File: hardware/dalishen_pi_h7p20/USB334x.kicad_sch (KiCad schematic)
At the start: 20 parts, among them J2 USB_C_Receptacle_USB2.0_16P, J3 USB_A, SW6 SW_DPDT_x2, U20 USB3343, Y1 26M

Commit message: [dalishen_pi_h7p20] Backup
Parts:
- added F4: SMD0805B100TFT, Fuse:Fuse_0805_2012Metric, symbol Device:Polyfuse
- SW6: footprint (none) -> Button_Switch_SMD:SW_DIP_SPSTx03_Slide_KingTek_DSHP03TJ_W5.25mm_P1.27mm_JPin
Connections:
- net T_VBUS: now also F4.1; no longer J2.A4 (VBUS), J2.A9 (VBUS), J2.B4 (VBUS), J2.B9 (VBUS), J3.1 (VBUS)
- new net: F4.2, J2.A4 (VBUS), J2.A9 (VBUS), J2.B4 (VBUS), J2.B9 (VBUS), J3.1 (VBUS)
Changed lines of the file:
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@@
 	(wire
 		(pts
-			(xy 146.05 53.34) (xy 120.65 53.34)
+			(xy 146.05 53.34) (xy 137.16 53.34)
 		)
 		(stroke
@@
 	(wire
 		(pts
+			(xy 129.54 53.34) (xy 120.65 53.34)
+		)
+		(stroke
+			(width 0)
+			(type default)
+		)
+	)
+	(wire
+		(pts
 			(xy 154.94 93.98) (xy 154.94 95.25)
 		)
@@
 	)
 	(label "T_VBUS"
-		(at 109.22 107.95 0)
+		(at 137.16 53.34 0)
 		(effects
 			(font
@@
 	)
 	(symbol
+		(lib_id "Device:Polyfuse")
+		(at 133.35 53.34 270)
+		(unit 1)
+		(exclude_from_sim no)
+		(in_bom yes)
+		(on_board yes)
+		(dnp no)
+		(property "Reference" "F4"
+			(at 133.35 47.625 90)
+			(effects
+				(font
+					(size 1.27 1.27)
+				)
+			)
+		)
+		(property "Value" "SMD0805B100TFT"
+			(at 133.35 49.9364 90)
+			(effects
+				(font
+					(size 1.27 1.27)
+				)
+			)
+		)
+		(property "Footprint" "Fuse:Fuse_0805_2012Metric"
+			(at 128.27 54.61 0)
+			(effects
+				(font
+					(size 1.27 1.27)
+				)
+				(justify left)
+				(hide yes)
+			)
+		)
+		(property "Datasheet" "~"
+			(at 133.35 53.34 0)
+			(effects
+				(font
+					(size 1.27 1.27)
+				)
+				(hide yes)
+			)
+		)
+		(property "Description" ""
+			(at 133.35 53.34 0)
+			(effects
+				(font
+					(size 1.27 1.27)
+				)
+			)
+		)
+		(pin "1"
+		)
+		(pin "2"
+		)
+		(instances
+			(project "dalishen_pi_h7p20"
+				(path "/221176f3-b6da-4f04-afa6-f8c6dd49907a/c2e39904-e110-4fb2-9a78-c219110dbd62"
+					(reference "F4")
+					(unit 1)
+				)
+			)
+		)
+	)
+	(symbol
 		(lib_id "Device:R")
 		(at 48.26 62.23 270)
@@
 			)
 		)
-		(property "Footprint" ""
+		(property "Footprint" "Button_Switch_SMD:SW_DIP_SPSTx03_Slide_KingTek_DSHP03TJ_W5.25mm_P1.27mm_JPin"
 			(at 38.1 59.69 0)
 			(effects
@@
 			)
 		)
-		(property "Footprint" ""
+		(property "Footprint" "Button_Switch_SMD:SW_DIP_SPSTx03_Slide_KingTek_DSHP03TJ_W5.25mm_P1.27mm_JPin"
 			(at 38.1 46.99 0)
 			(effects

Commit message: [dalishen_pi_h7p20] 待review
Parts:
- SW6: footprint Button_Switch_SMD:SW_DIP_SPSTx03_Slide_KingTek_DSHP03TJ_W5.25mm_P1.27mm_JPin -> vllogic:SW_PUSH_5.8mm_LOCK_SMT
- U20: footprint Package_DFN_QFN:QFN-24-1EP_4x4mm_P0.5mm_EP2.6x2.6mm -> vllogic:QFN-24-1EP_4x4mm_P0.5mm_EP2.6x2.6mm
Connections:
- net T_VBUS: now also R79.2; no longer R79.1
- net at U20.17 (VBUS): now also R79.1; no longer R79.2
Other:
- moved on the sheet: R79
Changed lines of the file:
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@@
 			)
 		)
-		(property "Footprint" "Button_Switch_SMD:SW_DIP_SPSTx03_Slide_KingTek_DSHP03TJ_W5.25mm_P1.27mm_JPin"
+		(property "Footprint" "vllogic:SW_PUSH_5.8mm_LOCK_SMT"
 			(at 38.1 59.69 0)
 			(effects
@@
 			)
 		)
-		(property "Footprint" "Package_DFN_QFN:QFN-24-1EP_4x4mm_P0.5mm_EP2.6x2.6mm"
+		(property "Footprint" "vllogic:QFN-24-1EP_4x4mm_P0.5mm_EP2.6x2.6mm"
 			(at 210.82 71.12 0)
 			(effects
@@
 	(symbol
 		(lib_id "Device:R")
-		(at 162.56 68.58 90)
+		(at 162.56 68.58 270)
+		(mirror x)
 		(unit 1)
 		(exclude_from_sim no)
@@
 			)
 		)
-		(property "Footprint" "Button_Switch_SMD:SW_DIP_SPSTx03_Slide_KingTek_DSHP03TJ_W5.25mm_P1.27mm_JPin"
+		(property "Footprint" "vllogic:SW_PUSH_5.8mm_LOCK_SMT"
 			(at 38.1 46.99 0)
 			(effects

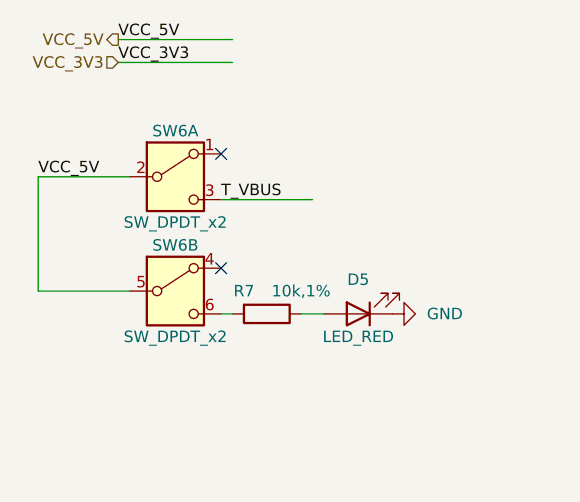
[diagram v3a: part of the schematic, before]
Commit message: [dalishen_pi_h7p20]自锁开关脚位修正
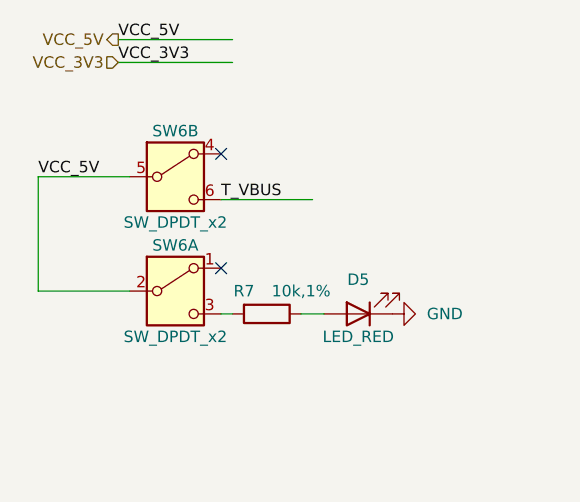
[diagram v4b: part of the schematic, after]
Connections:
- net T_VBUS: now also SW6.6 (C); no longer SW6.3 (C)
- net at R7.2: now also SW6.3 (C); no longer SW6.6 (C)
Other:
- moved on the sheet: SW6A, SW6B
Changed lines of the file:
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@@
 	(symbol
 		(lib_id "Switch:SW_DPDT_x2")
-		(at 38.1 59.69 0)
+		(at 38.1 46.99 0)
 		(unit 2)
 		(exclude_from_sim no)
@@
 		(dnp no)
 		(property "Reference" "SW6"
-			(at 38.1 54.61 0)
+			(at 38.1 41.91 0)
 			(effects
 				(font
@@
 		)
 		(property "Value" "SW_DPDT_x2"
-			(at 38.1 64.77 0)
+			(at 38.1 52.07 0)
 			(effects
 				(font
@@
 		)
 		(property "Footprint" "vllogic:SW_PUSH_5.8mm_LOCK_SMT"
-			(at 38.1 59.69 0)
+			(at 38.1 46.99 0)
 			(effects
 				(font
@@
 		)
 		(property "Datasheet" "~"
-			(at 38.1 59.69 0)
+			(at 38.1 46.99 0)
 			(effects
 				(font
@@
 		)
 		(property "Description" "Switch, dual pole double throw, separate symbols"
-			(at 38.1 59.69 0)
+			(at 38.1 46.99 0)
 			(effects
 				(font
@@
 	(symbol
 		(lib_id "Switch:SW_DPDT_x2")
-		(at 38.1 46.99 0)
+		(at 38.1 59.69 0)
 		(unit 1)
 		(exclude_from_sim no)
@@
 		(dnp no)
 		(property "Reference" "SW6"
-			(at 38.1 41.91 0)
+			(at 38.1 54.61 0)
 			(effects
 				(font
@@
 		)
 		(property "Value" "SW_DPDT_x2"
-			(at 38.1 52.07 0)
+			(at 38.1 64.77 0)
 			(effects
 				(font
@@
 		)
 		(property "Footprint" "vllogic:SW_PUSH_5.8mm_LOCK_SMT"
-			(at 38.1 46.99 0)
+			(at 38.1 59.69 0)
 			(effects
 				(font
@@
 		)
 		(property "Datasheet" "~"
-			(at 38.1 46.99 0)
+			(at 38.1 59.69 0)
 			(effects
 				(font
@@
 		)
 		(property "Description" "Switch, dual pole double throw, separate symbols"
-			(at 38.1 46.99 0)
-			(effects
-				(font
+			(at 38.1 59.69 0)
+			(effects
+				(font

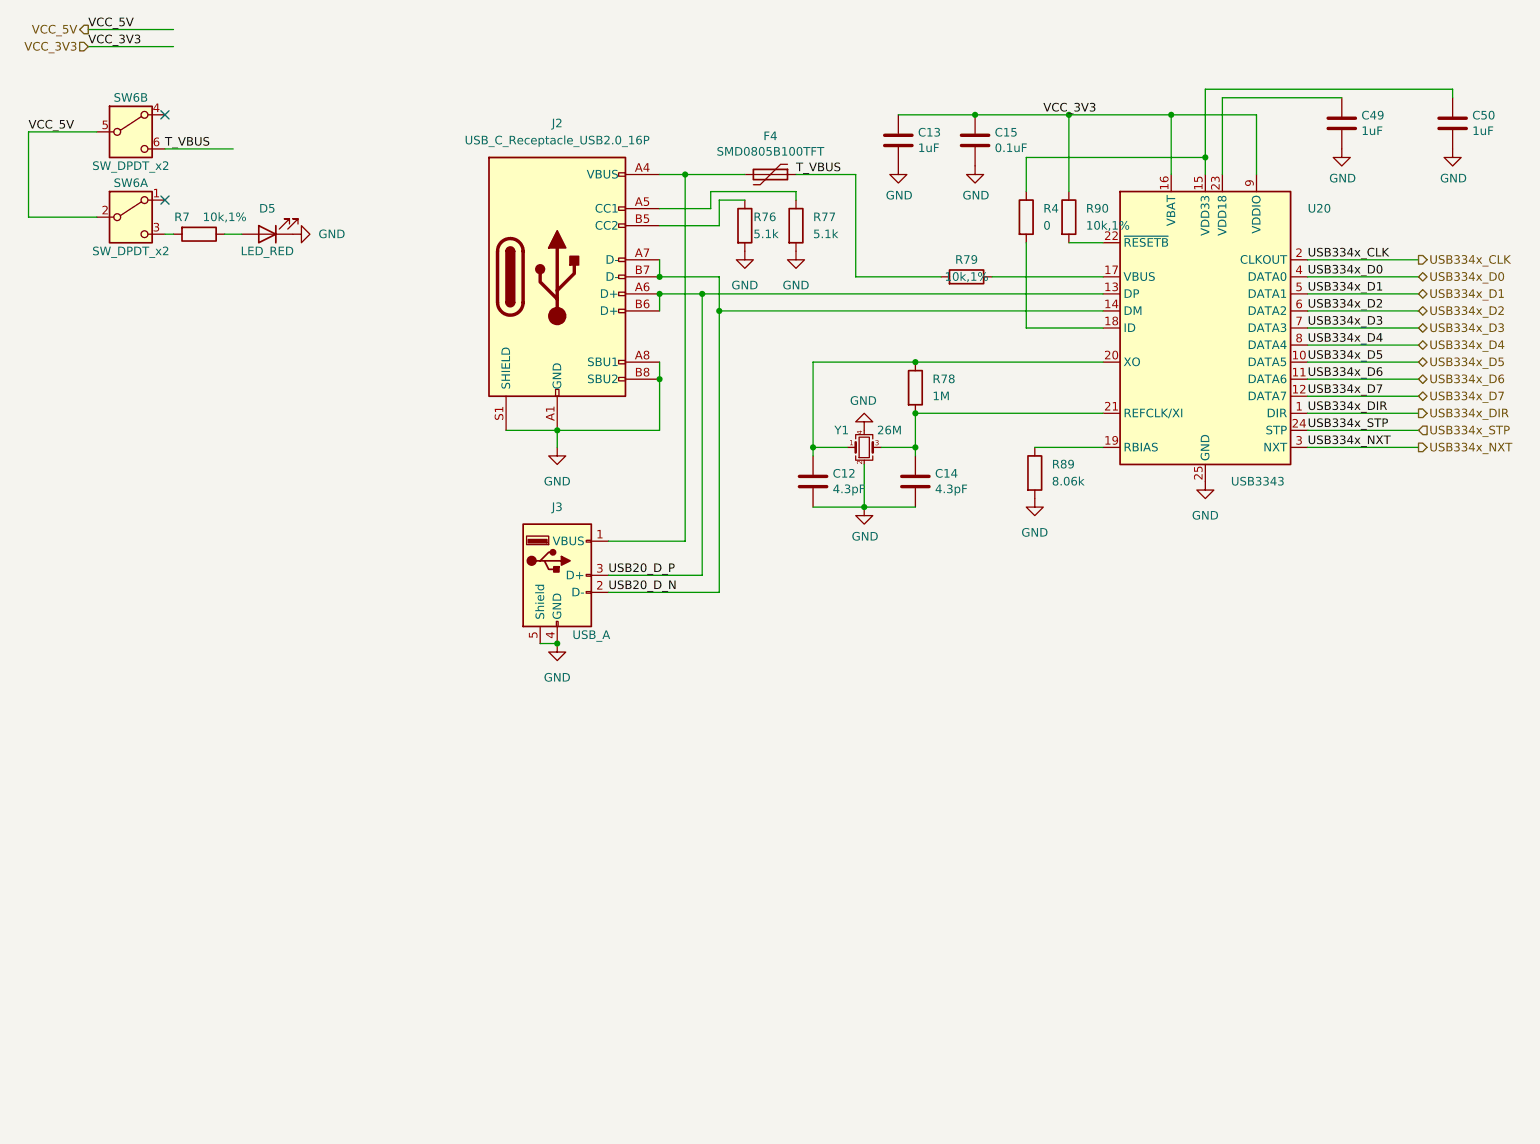
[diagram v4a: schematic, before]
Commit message: [dalishen_pi_h7p20] 生成方波
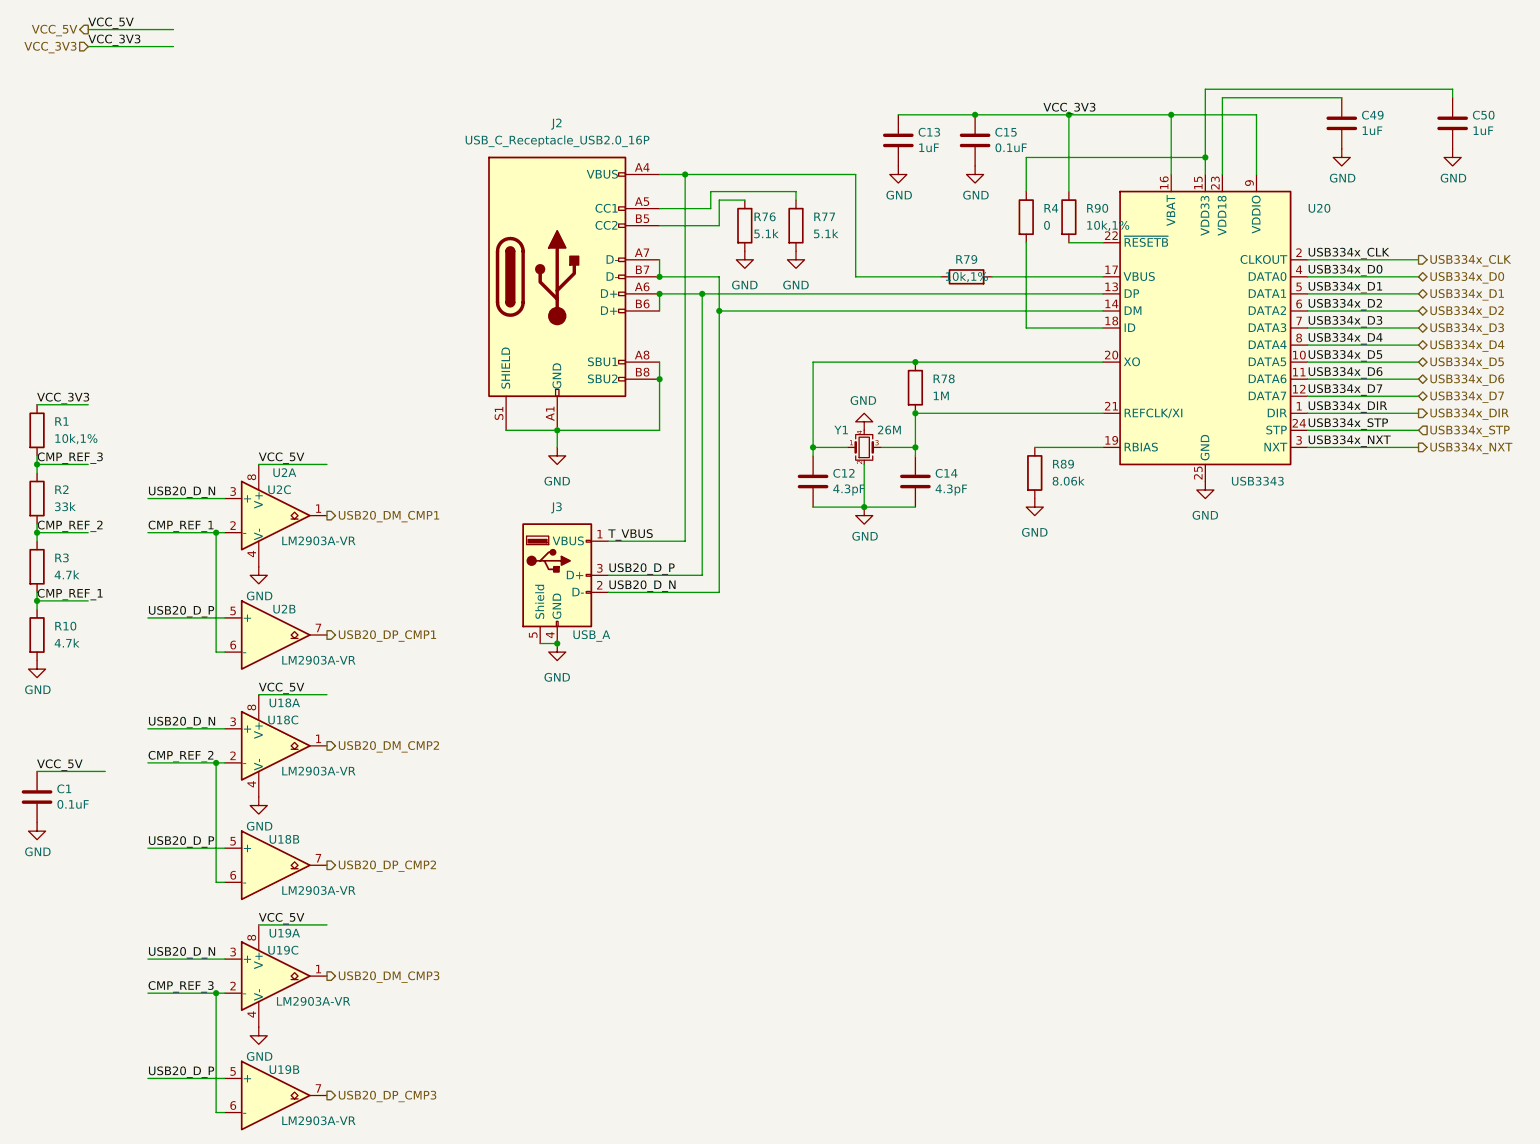
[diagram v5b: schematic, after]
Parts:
- removed D5: LED_RED, LED_SMD:LED_0603_1608Metric, symbol Device:LED
- removed F4: SMD0805B100TFT, Fuse:Fuse_0805_2012Metric, symbol Device:Polyfuse
- removed R7: 10k,1%, Resistor_SMD:R_0402_1005Metric, symbol Device:R
- removed SW6: SW_DPDT_x2, vllogic:SW_PUSH_5.8mm_LOCK_SMT, symbol Switch:SW_DPDT_x2
- added C1: 0.1uF, Capacitor_SMD:C_0402_1005Metric, symbol Device:C
- added R1: 10k,1%, Resistor_SMD:R_0402_1005Metric, symbol Device:R
- added R10, R3: 4.7k, Resistor_SMD:R_0402_1005Metric, symbol Device:R
- added R2: 33k, Resistor_SMD:R_0402_1005Metric, symbol Device:R
- added U18, U19, U2: LM2903A-VR, Package_SO:MSOP-8_3x3mm_P0.65mm, symbol Comparator:LM2903
- J3: footprint vllogic:USB_AF_SMT -> vllogic:USB-AF_YIJIAN
- U20: footprint vllogic:QFN-24-1EP_4x4mm_P0.5mm_EP2.6x2.6mm -> Package_DFN_QFN:QFN-24-1EP_4x4mm_P0.5mm_EP2.6x2.6mm
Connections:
- net GND: now also C1.1, R10.2, U18.4 (V-), U19.4 (V-), U2.4 (V-)
- net T_VBUS: now also J2.A4 (VBUS), J2.A9 (VBUS), J2.B4 (VBUS), J2.B9 (VBUS), J3.1 (VBUS), R79.1; no longer R79.2
- net USB20_D_N: now also U18.3 (+), U19.3 (+), U2.3 (+)
- net USB20_D_P: now also U18.5 (+), U19.5 (+), U2.5 (+)
- net VCC_3V3: now also R1.1
- net VCC_5V: now also C1.2, U18.8 (V+), U19.8 (V+), U2.8 (V+)
- net at U20.17 (VBUS): now also R79.2; no longer R79.1
- new net CMP_REF_1: R10.1, R3.2, U2.2 (-), U2.6 (-)
- new net CMP_REF_2: R2.2, R3.1, U18.2 (-), U18.6 (-)
- new net CMP_REF_3: R1.2, R2.1, U19.2 (-), U19.6 (-)
- new net USB20_DM_CMP1: U2.1
- new net USB20_DM_CMP2: U18.1
- new net USB20_DM_CMP3: U19.1
- new net USB20_DP_CMP1: U2.7
- new net USB20_DP_CMP2: U18.7
- new net USB20_DP_CMP3: U19.7
- no-connect marks 2 -> 0
